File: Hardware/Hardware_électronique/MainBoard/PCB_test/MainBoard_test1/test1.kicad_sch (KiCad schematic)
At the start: 30 parts, among them J1 Conn_RasPi, Q1 PMOS

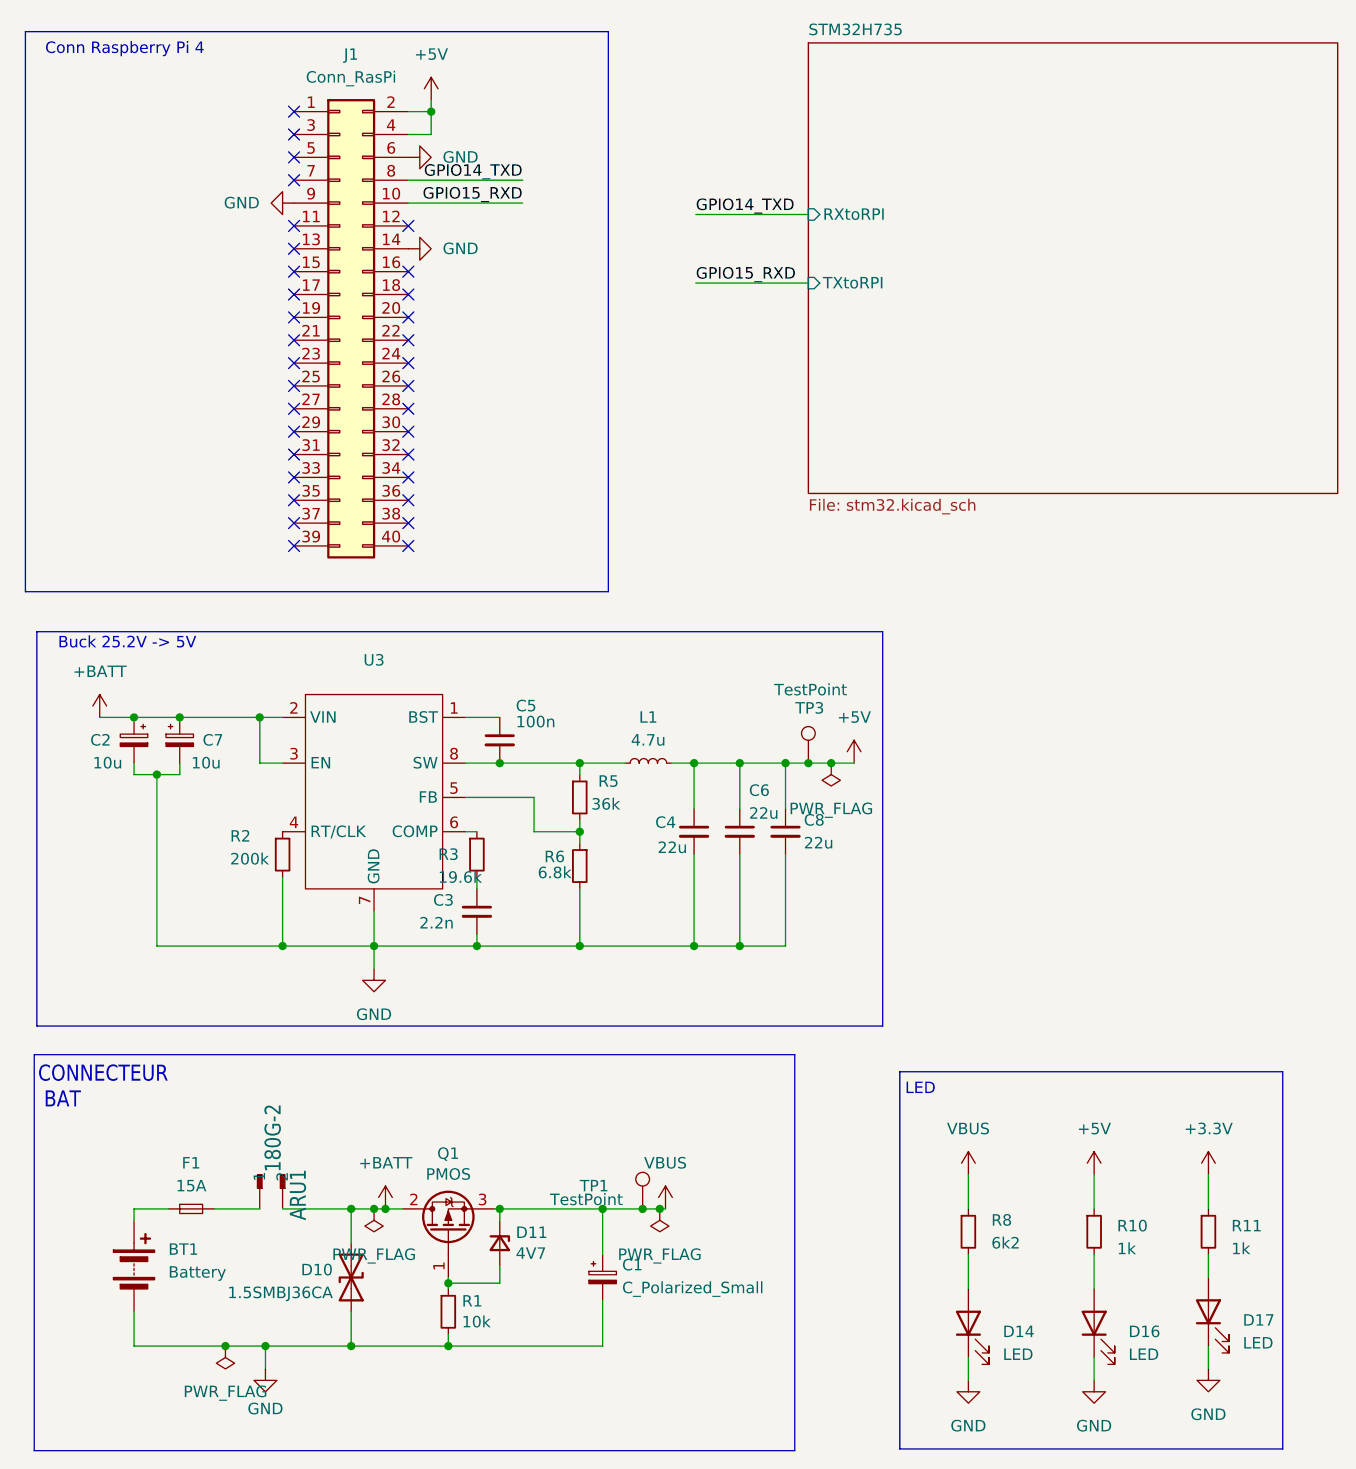
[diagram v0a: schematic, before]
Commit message: beginning of PCB design with Rpi4 shield shape
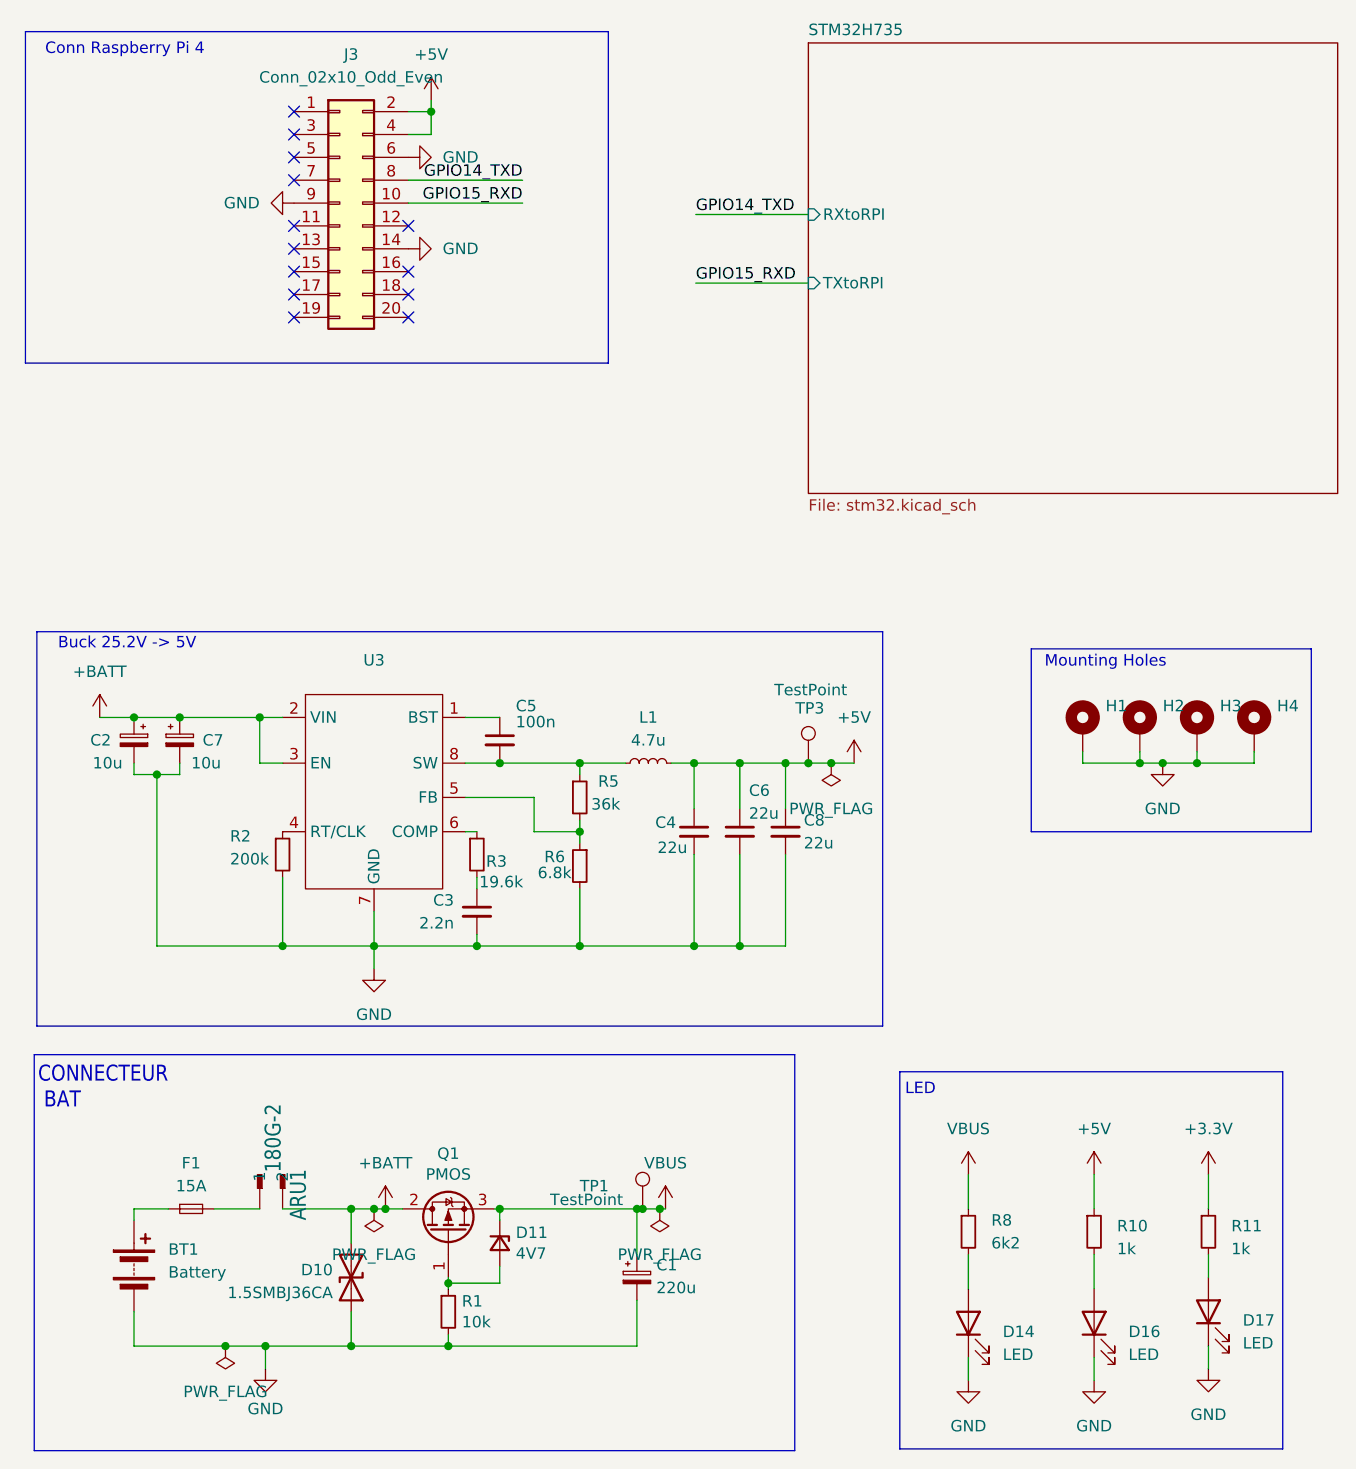
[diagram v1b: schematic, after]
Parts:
- removed J1: Conn_RasPi, Connector_PinSocket_2.54mm:PinSocket_2x20_P2.54mm_Vertical, symbol Connector_Generic:Conn_02x20_Odd_Even
- added H1, H2, H3, H4: MountingHole_Pad, MountingHole:MountingHole_2.7mm_M2.5, symbol Mechanical:MountingHole_Pad
- added J3: Conn_02x10_Odd_Even, Connector_PinSocket_2.54mm:PinSocket_2x10_P2.54mm_Vertical, symbol Connector_Generic:Conn_02x10_Odd_Even
- C1: value C_Polarized_Small -> 220u; footprint schematic1:E5-6 -> Capacitor_SMD:CP_Elec_10x10.5
- C5: footprint (none) -> Capacitor_SMD:C_0402_1005Metric_Pad0.74x0.62mm_HandSolder
- F1: footprint (none) -> Fuse:Fuse_1206_3216Metric_Pad1.42x1.75mm_HandSolder
- L1: footprint Inductor_SMD:L_Changjiang_FNR8065S -> MainBoard:PA5432.472NLT
- Q1: footprint schematic1:MOS_WDFN8 -> MainBoard:MOS_WDFN8
- R2, R5, R6: footprint (none) -> Resistor_SMD:R_0402_1005Metric_Pad0.72x0.64mm_HandSolder
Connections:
- net +5V: now also J3.2 (Pin_2), J3.4 (Pin_4)
- net GND: now also H1.1, H2.1, H3.1, H4.1, J3.14 (Pin_14), J3.6 (Pin_6), J3.9 (Pin_9)
- net GPIO14_TXD: now also J3.8 (Pin_8)
- net GPIO15_RXD: now also J3.10 (Pin_10)
- no-connect marks 33 -> 13
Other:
- note added: "Mounting Holes"
- moved on the sheet: C1

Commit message: MotherBoard finished
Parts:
- removed C2, C7: 10u, Capacitor_SMD:CP_Elec_4x5.4, symbol Device:C_Polarized_Small
- removed D14, D16, D17: LED, LED_SMD:LED_0603_1608Metric, symbol Device:LED
- removed R10, R11: 1k, Resistor_SMD:R_0402_1005Metric, symbol Device:R_Small
- removed R8: 6k2, Resistor_SMD:R_0402_1005Metric, symbol Device:R_Small
- added C2, C7: 10u, Capacitor_SMD:C_0805_2012Metric, symbol Device:C_Small
- C3: footprint Capacitor_SMD:C_0805_2012Metric_Pad1.18x1.45mm_HandSolder -> Capacitor_SMD:C_0402_1005Metric_Pad0.74x0.62mm_HandSolder
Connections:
- net +BATT: now also C2.1, C7.1
- net GND: now also C2.2, C7.2
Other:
- note removed: "LED"
- moved on the sheet: R2

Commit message: Updating t
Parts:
- C3, C5: footprint Capacitor_SMD:C_0402_1005Metric_Pad0.74x0.62mm_HandSolder -> Capacitor_SMD:C_0402_1005Metric
- C4, C6, C8: footprint Capacitor_SMD:C_0603_1608Metric_Pad1.08x0.95mm_HandSolder -> Capacitor_SMD:C_0402_1005Metric
- F1: footprint Fuse:Fuse_1206_3216Metric_Pad1.42x1.75mm_HandSolder -> Fuse:Fuse_1206_3216Metric
- R1: footprint Resistor_SMD:R_0805_2012Metric_Pad1.20x1.40mm_HandSolder -> Resistor_SMD:R_0402_1005Metric
- R2, R3, R5, R6: footprint Resistor_SMD:R_0402_1005Metric_Pad0.72x0.64mm_HandSolder -> Resistor_SMD:R_0402_1005Metric
